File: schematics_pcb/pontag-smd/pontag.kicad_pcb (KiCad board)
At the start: 2 copper layers, 36.8 x 44.5 mm, 32 parts, among them J1 Ext. VCC, J2 External 12V, J3 RS232 Port, J4 PS/2 Mouse, J5 AVR-ISP-6, J7 Extra, SW1 Reset, U1 LP2985-5.0, U3 ATmega8A-AU, U4 MAX232A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

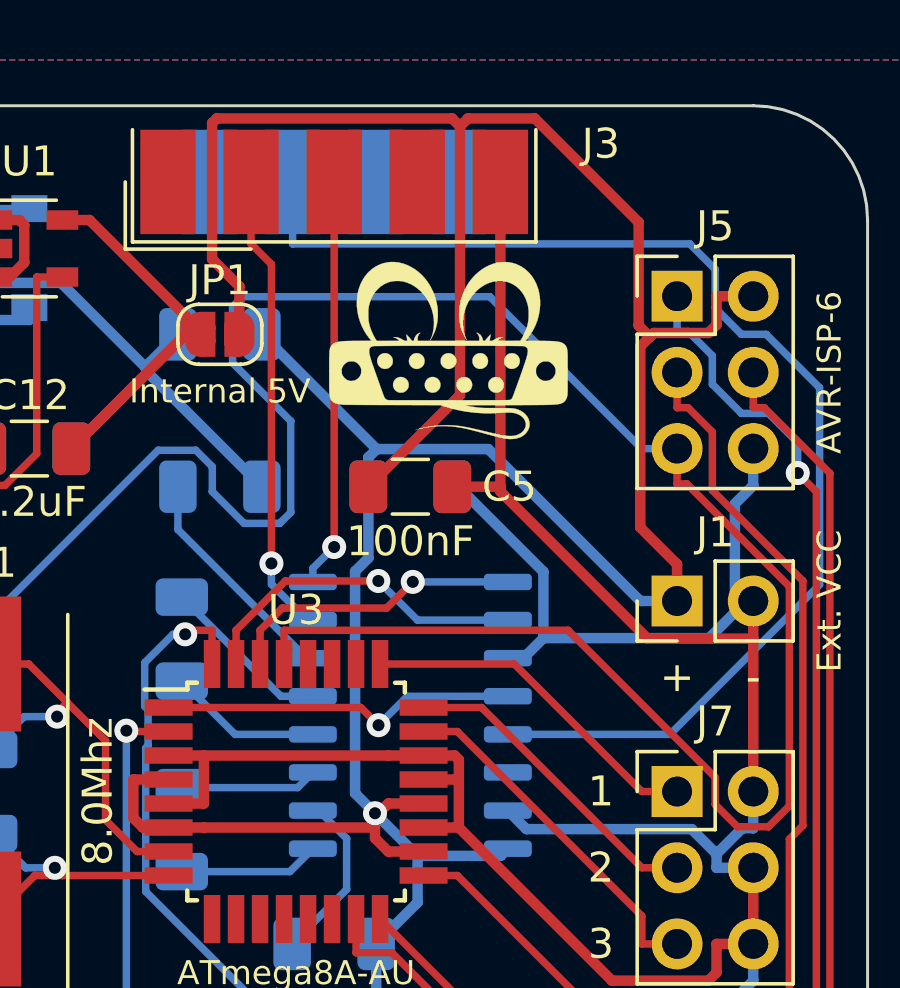
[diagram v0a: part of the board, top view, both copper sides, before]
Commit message: Rerouted some traces
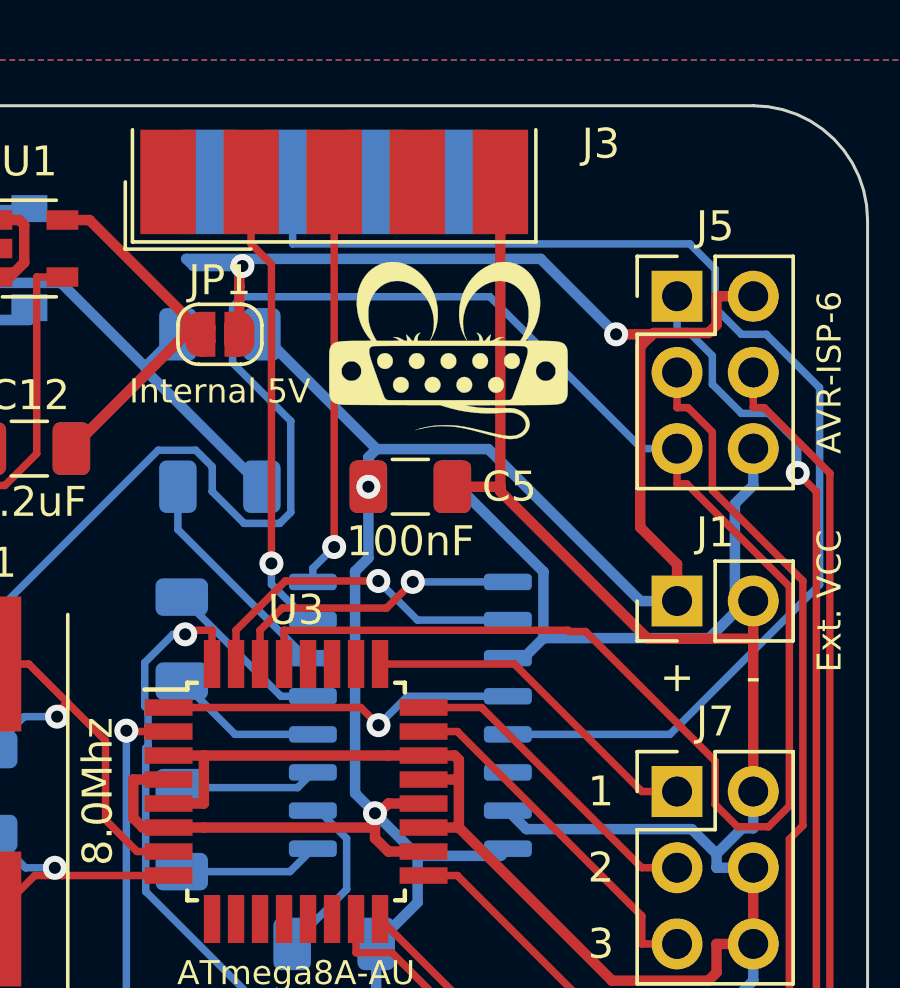
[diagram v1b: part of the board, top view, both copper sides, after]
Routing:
- net VCC: track 141.2 -> 121.4 mm, vias 2 -> 5
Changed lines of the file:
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@@
     (thickness 1.6)
     (drawings 16)
-    (tracks 362)
+    (tracks 364)
     (zones 0)
     (modules 32)
@@
     (add_net /PS2-DATA)
     (add_net /RESET)
-    (add_net /RS232-DTR)
     (add_net /RS232-RTS)
     (add_net /RS232-RX)
@@
     (add_net "Net-(D4-Pad2)")
     (add_net "Net-(D5-Pad1)")
-    (add_net "Net-(J3-Pad1)")
-    (add_net "Net-(J3-Pad6)")
-    (add_net "Net-(J3-Pad8)")
-    (add_net "Net-(J3-Pad9)")
-    (add_net "Net-(J4-Pad2)")
-    (add_net "Net-(J4-Pad6)")
     (add_net "Net-(J7-Pad1)")
     (add_net "Net-(J7-Pad3)")
     (add_net "Net-(J7-Pad5)")
-    (add_net "Net-(U3-Pad10)")
-    (add_net "Net-(U3-Pad11)")
-    (add_net "Net-(U3-Pad12)")
-    (add_net "Net-(U3-Pad13)")
-    (add_net "Net-(U3-Pad14)")
-    (add_net "Net-(U3-Pad26)")
-    (add_net "Net-(U3-Pad27)")
-    (add_net "Net-(U3-Pad28)")
-    (add_net "Net-(U3-Pad9)")
-    (add_net "Net-(U4-Pad14)")
   )
   (net_class Power ""
@@
   (segment (start 95.0255 104.0954) (end 95.2947 103.8262) (width 0.35) (layer F.Cu) (net 6))
   (segment (start 95.2947 103.8262) (end 95.2947 102.87) (width 0.35) (layer F.Cu) (net 6))
-  (segment (start 86.7448 97.2083) (end 87.0085 96.9446) (width 0.35) (layer F.Cu) (net 6))
-  (segment (start 87.0085 96.9446) (end 89.2399 96.9446) (width 0.35) (layer F.Cu) (net 6))
-  (segment (start 89.2399 96.9446) (end 92.698 100.4027) (width 0.35) (layer F.Cu) (net 6))
-  (segment (start 92.698 100.4027) (end 92.698 103.8466) (width 0.35) (layer F.Cu) (net 6))
-  (segment (start 92.698 103.8466) (end 93.0739 104.2225) (width 0.35) (layer F.Cu) (net 6))
   (segment (start 93.98 111.8047) (end 92.7525 110.5772) (width 0.35) (layer F.Cu) (net 6))
   (segment (start 92.7525 110.5772) (end 92.7525 104.5439) (width 0.35) (layer F.Cu) (net 6))
   (segment (start 92.7525 104.5439) (end 93.0739 104.2225) (width 0.35) (layer F.Cu) (net 6))
-  (segment (start 86.7448 97.2083) (end 86.4811 96.9446) (width 0.35) (layer F.Cu) (net 6))
-  (segment (start 86.4811 96.9446) (end 78.6356 96.9446) (width 0.35) (layer F.Cu) (net 6))
-  (segment (start 78.6356 96.9446) (end 78.4813 97.0989) (width 0.35) (layer F.Cu) (net 6))
-  (segment (start 78.4813 97.0989) (end 78.4813 101.6318) (width 0.35) (layer F.Cu) (net 6))
-  (segment (start 78.4813 101.6318) (end 79.39 102.5405) (width 0.35) (layer F.Cu) (net 6))
   (segment (start 79.39 102.5405) (end 79.39 104.14) (width 0.35) (layer F.Cu) (net 6))
-  (segment (start 83.69 109.22) (end 86.7448 106.1652) (width 0.35) (layer F.Cu) (net 6))
-  (segment (start 86.7448 106.1652) (end 86.7448 97.2083) (width 0.35) (layer F.Cu) (net 6))
   (segment (start 96.52 102.87) (end 95.2947 102.87) (width 0.35) (layer F.Cu) (net 6))
   (segment (start 93.98 113.03) (end 93.98 111.8047) (width 0.35) (layer F.Cu) (net 6))
-  (segment (start 83.69 109.22) (end 83.69 111.5979) (width 0.35) (layer B.Cu) (net 6))
+  (segment (start 83.69 109.22) (end 83.69 109.22) (width 0.35) (layer B.Cu) (net 6))
   (segment (start 83.69 111.5979) (end 83.247 112.0409) (width 0.35) (layer B.Cu) (net 6))
   (segment (start 83.247 112.0409) (end 83.247 119.4402) (width 0.35) (layer B.Cu) (net 6))
@@
   (via (at 83.9105 120.1037) (size 0.8) (layers F.Cu B.Cu) (net 6))
   (via (at 84.8815 126.9229) (size 0.8) (layers F.Cu B.Cu) (net 6))
+  (via (at 79.492697 101.863303) (size 0.8) (drill 0.4) (layers F.Cu B.Cu) (net 6))
+  (segment (start 79.39 101.966) (end 79.492697 101.863303) (width 0.35) (layer F.Cu) (net 6))
+  (segment (start 79.39 102.5405) (end 79.39 101.966) (width 0.35) (layer F.Cu) (net 6))
+  (segment (start 89.43331 101.62531) (end 91.948 104.14) (width 0.35) (layer B.Cu) (net 6))
+  (segment (start 77.621975 101.62531) (end 89.43331 101.62531) (width 0.35) (layer B.Cu) (net 6))
+  (via (at 91.948 104.14) (size 0.8) (drill 0.4) (layers F.Cu B.Cu) (net 6))
+  (segment (start 77.859968 101.863303) (end 77.621975 101.62531) (width 0.35) (layer B.Cu) (net 6))
+  (segment (start 79.492697 101.863303) (end 77.859968 101.863303) (width 0.35) (layer B.Cu) (net 6))
+  (segment (start 92.9914 104.14) (end 93.0739 104.2225) (width 0.35) (layer F.Cu) (net 6))
+  (segment (start 91.948 104.14) (end 92.9914 104.14) (width 0.35) (layer F.Cu) (net 6))
+  (segment (start 83.69 109.22) (end 83.69 111.5979) (width 0.35) (layer B.Cu) (net 6))
+  (via (at 83.69 109.22) (size 0.8) (drill 0.4) (layers F.Cu B.Cu) (net 6))
   (segment (start 77.47 119.25) (end 81.335 119.25) (width 0.25) (layer B.Cu) (net 7))
   (segment (start 81.335 119.25) (end 81.84 118.745) (width 0.25) (layer B.Cu) (net 7))
@@
   (segment (start 83.82 134.62) (end 82.6947 134.62) (width 0.25) (layer B.Cu) (net 20))
   (via (at 75.6228 117.3513) (size 0.8) (layers F.Cu B.Cu) (net 20))
-  (segment (start 80.88 115.13) (end 80.88 114.0047) (width 0.25) (layer F.Cu) (net 21))
-  (segment (start 93.98 107.95) (end 93.98 109.1253) (width 0.25) (layer F.Cu) (net 21))
-  (segment (start 93.98 109.1253) (end 94.3036 109.1253) (width 0.25) (layer F.Cu) (net 21))
-  (segment (start 94.3036 109.1253) (end 97.7229 112.5446) (width 0.25) (layer F.Cu) (net 21))
-  (segment (start 97.7229 112.5446) (end 97.7229 119.8621) (width 0.25) (layer F.Cu) (net 21))
-  (segment (start 97.7229 119.8621) (end 97.0296 120.5554) (width 0.25) (layer F.Cu) (net 21))
-  (segment (start 97.0296 120.5554) (end 95.9944 120.5554) (width 0.25) (layer F.Cu) (net 21))
-  (segment (start 95.9944 120.5554) (end 95.25 119.811) (width 0.25) (layer F.Cu) (net 21))
-  (segment (start 95.25 119.811) (end 95.25 118.9073) (width 0.25) (layer F.Cu) (net 21))
-  (segment (start 95.25 118.9073) (end 90.3474 114.0047) (width 0.25) (layer F.Cu) (net 21))
-  (segment (start 90.3474 114.0047) (end 80.88 114.0047) (width 0.25) (layer F.Cu) (net 21))
   (segment (start 92.8047 107.95) (end 87.7424 102.8877) (width 0.25) (layer B.Cu) (net 21))
   (segment (start 87.7424 102.8877) (end 79.4951 102.8877) (width 0.25) (layer B.Cu) (net 21))
@@
   (segment (start 67.31 136.0058) (end 67.31 134.75) (width 0.25) (layer B.Cu) (net 21))
   (via (at 67.31 136.0058) (size 0.8) (layers F.Cu B.Cu) (net 21))
+  (segment (start 90.3474 114.0047) (end 80.88 114.0047) (width 0.25) (layer F.Cu) (net 21))
+  (segment (start 90.389698 114.046998) (end 90.3474 114.0047) (width 0.25) (layer F.Cu) (net 21))
+  (segment (start 95.25 118.364998) (end 90.932 114.046998) (width 0.25) (layer F.Cu) (net 21))
+  (segment (start 95.25 119.811) (end 95.25 118.364998) (width 0.25) (layer F.Cu) (net 21))
+  (segment (start 80.88 114.0047) (end 80.88 115.13) (width 0.25) (layer F.Cu) (net 21))
+  (segment (start 90.932 114.046998) (end 90.389698 114.046998) (width 0.25) (layer F.Cu) (net 21))
+  (segment (start 95.9944 120.5554) (end 95.25 119.811) (width 0.25) (layer F.Cu) (net 21))
+  (segment (start 97.7229 119.8621) (end 97.0296 120.5554) (width 0.25) (layer F.Cu) (net 21))
+  (segment (start 97.7229 112.5446) (end 97.7229 119.8621) (width 0.25) (layer F.Cu) (net 21))
+  (segment (start 97.0296 120.5554) (end 95.9944 120.5554) (width 0.25) (layer F.Cu) (net 21))
+  (segment (start 94.3036 109.1253) (end 97.7229 112.5446) (width 0.25) (layer F.Cu) (net 21))
+  (segment (start 93.98 109.1253) (end 94.3036 109.1253) (width 0.25) (layer F.Cu) (net 21))
+  (segment (start 93.98 107.95) (end 93.98 109.1253) (width 0.25) (layer F.Cu) (net 21))
   (segment (start 83.28 124.7553) (end 84.4774 124.7553) (width 0.25) (layer F.Cu) (net 22))
   (segment (start 84.4774 124.7553) (end 93.1116 133.3895) (width 0.25) (layer F.Cu) (net 22))
